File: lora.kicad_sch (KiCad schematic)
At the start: 2 parts

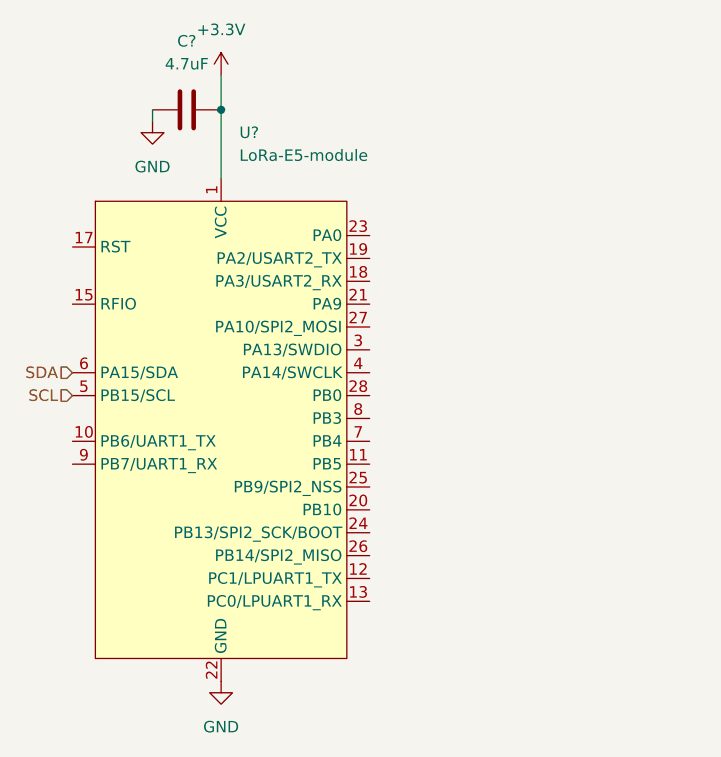
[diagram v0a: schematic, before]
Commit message: Added new lora, added rgb leds, updated TSP65988 schematic, added bat to 3v3, added battery balancer
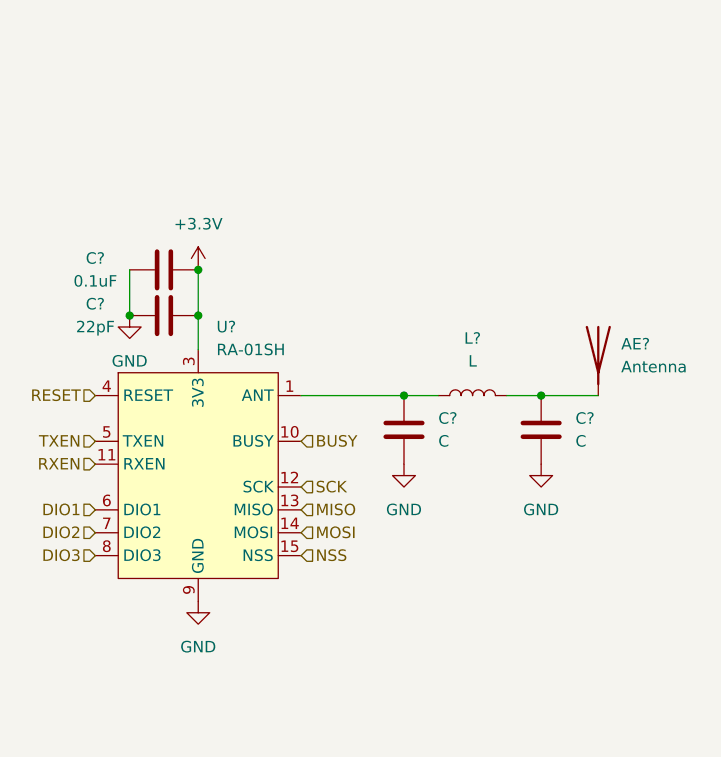
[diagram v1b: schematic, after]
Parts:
- removed C?: 4.7uF, symbol Device:C
- removed U?: LoRa-E5-module, airsoft_controller:LoRa-E5-module, symbol airsoft_controller:LoRa-E5-module
- added AE?: Antenna, symbol Device:Antenna
- added C?: 22pF, symbol Device:C
- added C? (x2): C, symbol Device:C
- added C?: 0.1uF, symbol Device:C
- added L?: L, symbol Device:L
- added U?: RA-01SH, symbol airsoft_controller:RA-01SH
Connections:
- net +3.3V: now also C?.2, C?.2, U?.3 (3V3)
- net GND: now also C?.1, C?.1, C?.2, C?.2, U?.16 (GND), U?.2 (GND), U?.9 (GND)
- new net: AE?.1 (A), C?.1, L?.2
- new net: C?.1, L?.1, U?.1 (ANT)
- new net BUSY: U?.10 (BUSY)
- new net DIO1: U?.6 (DIO1)
- new net DIO2: U?.7 (DIO2)
- new net DIO3: U?.8 (DIO3)
- new net MISO: U?.13 (MISO)
- new net MOSI: U?.14 (MOSI)
- new net NSS: U?.15 (NSS)
- new net RESET: U?.4 (RESET)
- new net RXEN: U?.11 (RXEN)
- new net SCK: U?.12 (SCK)
- new net TXEN: U?.5 (TXEN)

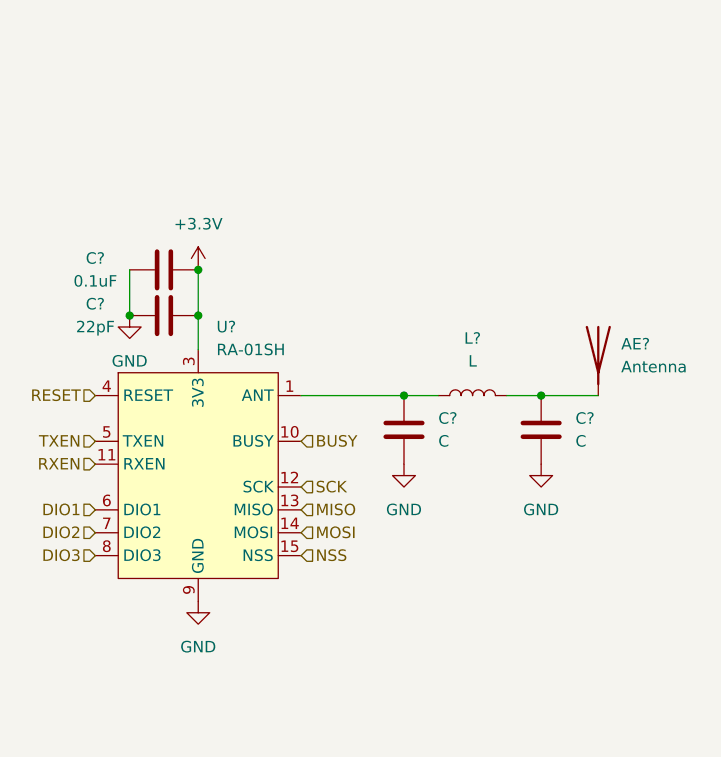
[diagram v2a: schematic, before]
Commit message: added audio ref schematic, added bat to 5V, added shift register, connected devices with other periferals
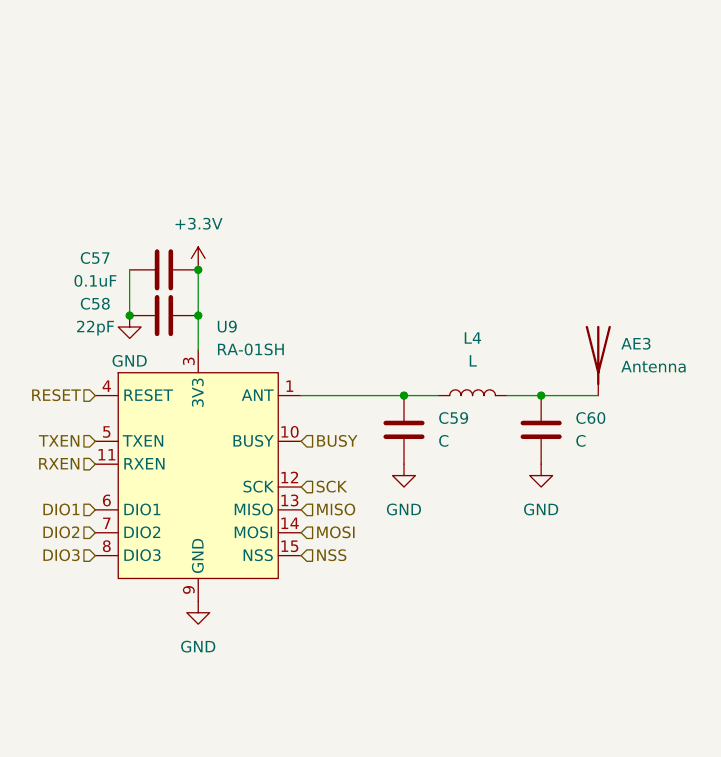
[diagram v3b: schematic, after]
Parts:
- gave numbers to parts that had none: 7
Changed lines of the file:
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@@
   (symbol (lib_id "Device:C") (at 143.51 83.82 90) (unit 1)
     (in_bom yes) (on_board yes)
-    (property "Reference" "C?" (id 0) (at 135.89 82.55 90))
+    (property "Reference" "C58" (id 0) (at 135.89 82.55 90))
     (property "Value" "22pF" (id 1) (at 135.89 85.09 90))
     (property "Footprint" "" (id 2) (at 147.32 82.8548 0)
@@
   (symbol (lib_id "Device:C") (at 185.42 96.52 0) (unit 1)
     (in_bom yes) (on_board yes) (fields_autoplaced)
-    (property "Reference" "C?" (id 0) (at 189.23 95.2499 0)
+    (property "Reference" "C60" (id 0) (at 189.23 95.2499 0)
       (effects (font (size 1.27 1.27)) (justify left))
     )
@@
   (symbol (lib_id "Device:Antenna") (at 191.77 87.63 0) (unit 1)
     (in_bom yes) (on_board yes) (fields_autoplaced)
-    (property "Reference" "AE?" (id 0) (at 194.31 86.9949 0)
+    (property "Reference" "AE3" (id 0) (at 194.31 86.9949 0)
       (effects (font (size 1.27 1.27)) (justify left))
     )
@@
   (symbol (lib_id "Device:C") (at 143.51 78.74 90) (unit 1)
     (in_bom yes) (on_board yes)
-    (property "Reference" "C?" (id 0) (at 135.89 77.47 90))
+    (property "Reference" "C57" (id 0) (at 135.89 77.47 90))
     (property "Value" "0.1uF" (id 1) (at 135.89 80.01 90))
     (property "Footprint" "" (id 2) (at 147.32 77.7748 0)
@@
   (symbol (lib_id "Device:C") (at 170.18 96.52 0) (unit 1)
     (in_bom yes) (on_board yes) (fields_autoplaced)
-    (property "Reference" "C?" (id 0) (at 173.99 95.2499 0)
+    (property "Reference" "C59" (id 0) (at 173.99 95.2499 0)
       (effects (font (size 1.27 1.27)) (justify left))
     )
@@
   (symbol (lib_id "Device:L") (at 177.8 92.71 90) (unit 1)
     (in_bom yes) (on_board yes) (fields_autoplaced)
-    (property "Reference" "L?" (id 0) (at 177.8 86.36 90))
+    (property "Reference" "L4" (id 0) (at 177.8 86.36 90))
     (property "Value" "L" (id 1) (at 177.8 88.9 90))
     (property "Footprint" "" (id 2) (at 177.8 92.71 0)
@@
   (symbol (lib_id "airsoft_controller:RA-01SH") (at 147.32 101.6 0) (unit 1)
     (in_bom yes) (on_board yes) (fields_autoplaced)
-    (property "Reference" "U?" (id 0) (at 149.3394 85.09 0)
+    (property "Reference" "U9" (id 0) (at 149.3394 85.09 0)
       (effects (font (size 1.27 1.27)) (justify left))
     )
@@
       (effects (font (size 1.27 1.27)) hide)
     )
-    (property "Datasheet" "" (id 3) (at 147.32 101.6 0)
+    (property "Datasheet" "https://docs.ai-thinker.com/_media/lora/docs/ra-01sh_specification.pdf" (id 3) (at 147.32 101.6 0)
       (effects (font (size 1.27 1.27)) hide)
     )

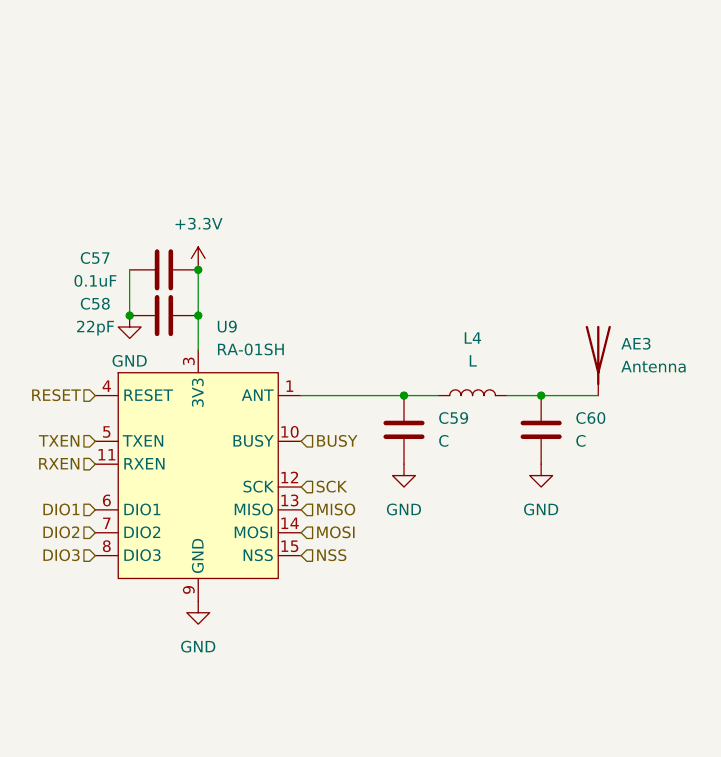
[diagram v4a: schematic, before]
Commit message: minor optimized pinassignement, added capacitors, added connectors
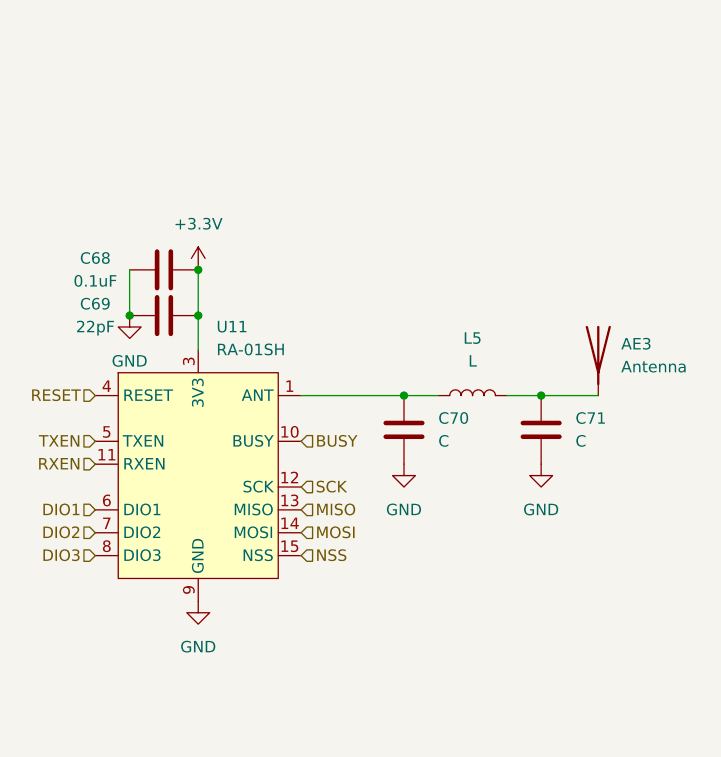
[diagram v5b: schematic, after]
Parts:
- renumbered C57 to C68, C58 to C69, C59 to C70, C60 to C71, L4 to L5, U9 to U11
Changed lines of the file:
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@@
   (symbol (lib_id "power:GND") (at 147.32 115.57 0) (unit 1)
     (in_bom yes) (on_board yes) (fields_autoplaced)
-    (property "Reference" "#PWR0172" (id 0) (at 147.32 121.92 0)
+    (property "Reference" "#PWR088" (id 0) (at 147.32 121.92 0)
       (effects (font (size 1.27 1.27)) hide)
     )
@@
   (symbol (lib_id "Device:C") (at 143.51 83.82 90) (unit 1)
     (in_bom yes) (on_board yes)
-    (property "Reference" "C58" (id 0) (at 135.89 82.55 90))
+    (property "Reference" "C69" (id 0) (at 135.89 82.55 90))
     (property "Value" "22pF" (id 1) (at 135.89 85.09 90))
     (property "Footprint" "" (id 2) (at 147.32 82.8548 0)
@@
   (symbol (lib_id "power:GND") (at 170.18 100.33 0) (unit 1)
     (in_bom yes) (on_board yes) (fields_autoplaced)
-    (property "Reference" "#PWR0169" (id 0) (at 170.18 106.68 0)
+    (property "Reference" "#PWR089" (id 0) (at 170.18 106.68 0)
       (effects (font (size 1.27 1.27)) hide)
     )
@@
   (symbol (lib_id "Device:C") (at 185.42 96.52 0) (unit 1)
     (in_bom yes) (on_board yes) (fields_autoplaced)
-    (property "Reference" "C60" (id 0) (at 189.23 95.2499 0)
+    (property "Reference" "C71" (id 0) (at 189.23 95.2499 0)
       (effects (font (size 1.27 1.27)) (justify left))
     )
@@
   (symbol (lib_id "power:GND") (at 185.42 100.33 0) (unit 1)
     (in_bom yes) (on_board yes) (fields_autoplaced)
-    (property "Reference" "#PWR0170" (id 0) (at 185.42 106.68 0)
+    (property "Reference" "#PWR090" (id 0) (at 185.42 106.68 0)
       (effects (font (size 1.27 1.27)) hide)
     )
@@
   (symbol (lib_id "power:GND") (at 139.7 83.82 0) (unit 1)
     (in_bom yes) (on_board yes) (fields_autoplaced)
-    (property "Reference" "#PWR0173" (id 0) (at 139.7 90.17 0)
+    (property "Reference" "#PWR086" (id 0) (at 139.7 90.17 0)
       (effects (font (size 1.27 1.27)) hide)
     )
@@
   (symbol (lib_id "Device:C") (at 143.51 78.74 90) (unit 1)
     (in_bom yes) (on_board yes)
-    (property "Reference" "C57" (id 0) (at 135.89 77.47 90))
+    (property "Reference" "C68" (id 0) (at 135.89 77.47 90))
     (property "Value" "0.1uF" (id 1) (at 135.89 80.01 90))
     (property "Footprint" "" (id 2) (at 147.32 77.7748 0)
@@
   (symbol (lib_id "Device:C") (at 170.18 96.52 0) (unit 1)
     (in_bom yes) (on_board yes) (fields_autoplaced)
-    (property "Reference" "C59" (id 0) (at 173.99 95.2499 0)
+    (property "Reference" "C70" (id 0) (at 173.99 95.2499 0)
       (effects (font (size 1.27 1.27)) (justify left))
     )
@@
   (symbol (lib_id "power:+3.3V") (at 147.32 78.74 0) (unit 1)
     (in_bom yes) (on_board yes) (fields_autoplaced)
-    (property "Reference" "#PWR0171" (id 0) (at 147.32 82.55 0)
+    (property "Reference" "#PWR087" (id 0) (at 147.32 82.55 0)
       (effects (font (size 1.27 1.27)) hide)
     )
@@
   (symbol (lib_id "Device:L") (at 177.8 92.71 90) (unit 1)
     (in_bom yes) (on_board yes) (fields_autoplaced)
-    (property "Reference" "L4" (id 0) (at 177.8 86.36 90))
+    (property "Reference" "L5" (id 0) (at 177.8 86.36 90))
     (property "Value" "L" (id 1) (at 177.8 88.9 90))
     (property "Footprint" "" (id 2) (at 177.8 92.71 0)
@@
   (symbol (lib_id "airsoft_controller:RA-01SH") (at 147.32 101.6 0) (unit 1)
     (in_bom yes) (on_board yes) (fields_autoplaced)
-    (property "Reference" "U9" (id 0) (at 149.3394 85.09 0)
+    (property "Reference" "U11" (id 0) (at 149.3394 85.09 0)
       (effects (font (size 1.27 1.27)) (justify left))
     )

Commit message: PI LC lowpass filter, added CP2012 reset, added connectors
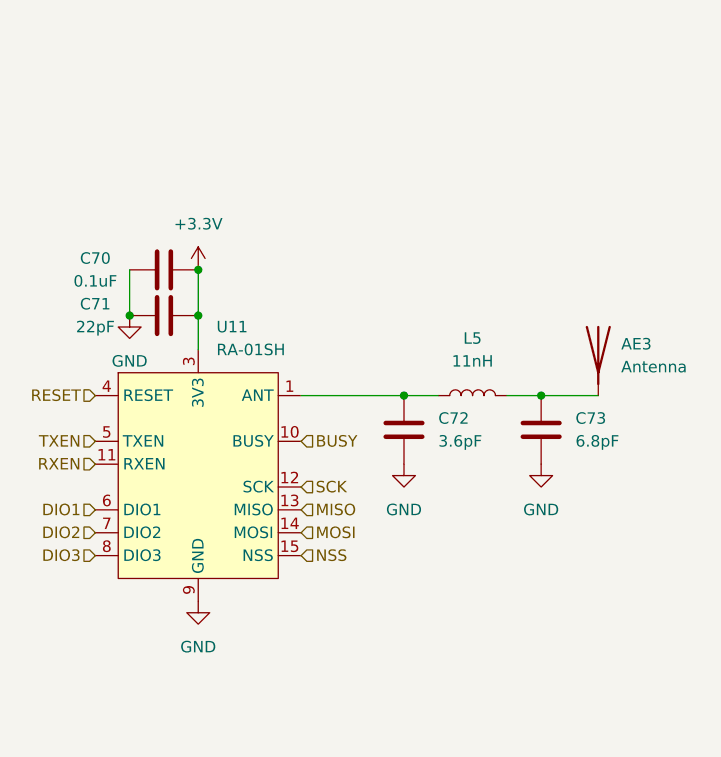
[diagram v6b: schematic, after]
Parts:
- C72: renamed from C70; value C -> 3.6pF
- C73: renamed from C71; value C -> 6.8pF
- L5: value L -> 11nH
- renumbered C68 to C70, C69 to C71
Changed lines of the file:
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@@
   (symbol (lib_id "power:GND") (at 147.32 115.57 0) (unit 1)
     (in_bom yes) (on_board yes) (fields_autoplaced)
-    (property "Reference" "#PWR088" (id 0) (at 147.32 121.92 0)
+    (property "Reference" "#PWR087" (id 0) (at 147.32 121.92 0)
       (effects (font (size 1.27 1.27)) hide)
     )
@@
   (symbol (lib_id "Device:C") (at 143.51 83.82 90) (unit 1)
     (in_bom yes) (on_board yes)
-    (property "Reference" "C69" (id 0) (at 135.89 82.55 90))
+    (property "Reference" "C71" (id 0) (at 135.89 82.55 90))
     (property "Value" "22pF" (id 1) (at 135.89 85.09 90))
     (property "Footprint" "" (id 2) (at 147.32 82.8548 0)
@@
   (symbol (lib_id "power:GND") (at 170.18 100.33 0) (unit 1)
     (in_bom yes) (on_board yes) (fields_autoplaced)
-    (property "Reference" "#PWR089" (id 0) (at 170.18 106.68 0)
+    (property "Reference" "#PWR088" (id 0) (at 170.18 106.68 0)
       (effects (font (size 1.27 1.27)) hide)
     )
@@
   (symbol (lib_id "Device:C") (at 185.42 96.52 0) (unit 1)
     (in_bom yes) (on_board yes) (fields_autoplaced)
-    (property "Reference" "C71" (id 0) (at 189.23 95.2499 0)
+    (property "Reference" "C73" (id 0) (at 189.23 95.2499 0)
       (effects (font (size 1.27 1.27)) (justify left))
     )
-    (property "Value" "C" (id 1) (at 189.23 97.7899 0)
+    (property "Value" "6.8pF" (id 1) (at 189.23 97.7899 0)
       (effects (font (size 1.27 1.27)) (justify left))
     )
@@
   (symbol (lib_id "power:GND") (at 185.42 100.33 0) (unit 1)
     (in_bom yes) (on_board yes) (fields_autoplaced)
-    (property "Reference" "#PWR090" (id 0) (at 185.42 106.68 0)
+    (property "Reference" "#PWR089" (id 0) (at 185.42 106.68 0)
       (effects (font (size 1.27 1.27)) hide)
     )
@@
   (symbol (lib_id "power:GND") (at 139.7 83.82 0) (unit 1)
     (in_bom yes) (on_board yes) (fields_autoplaced)
-    (property "Reference" "#PWR086" (id 0) (at 139.7 90.17 0)
+    (property "Reference" "#PWR085" (id 0) (at 139.7 90.17 0)
       (effects (font (size 1.27 1.27)) hide)
     )
@@
   (symbol (lib_id "Device:C") (at 143.51 78.74 90) (unit 1)
     (in_bom yes) (on_board yes)
-    (property "Reference" "C68" (id 0) (at 135.89 77.47 90))
+    (property "Reference" "C70" (id 0) (at 135.89 77.47 90))
     (property "Value" "0.1uF" (id 1) (at 135.89 80.01 90))
     (property "Footprint" "" (id 2) (at 147.32 77.7748 0)
@@
   (symbol (lib_id "Device:C") (at 170.18 96.52 0) (unit 1)
     (in_bom yes) (on_board yes) (fields_autoplaced)
-    (property "Reference" "C70" (id 0) (at 173.99 95.2499 0)
+    (property "Reference" "C72" (id 0) (at 173.99 95.2499 0)
       (effects (font (size 1.27 1.27)) (justify left))
     )
-    (property "Value" "C" (id 1) (at 173.99 97.7899 0)
+    (property "Value" "3.6pF" (id 1) (at 173.99 97.7899 0)
       (effects (font (size 1.27 1.27)) (justify left))
     )
@@
   (symbol (lib_id "power:+3.3V") (at 147.32 78.74 0) (unit 1)
     (in_bom yes) (on_board yes) (fields_autoplaced)
-    (property "Reference" "#PWR087" (id 0) (at 147.32 82.55 0)
+    (property "Reference" "#PWR086" (id 0) (at 147.32 82.55 0)
       (effects (font (size 1.27 1.27)) hide)
     )
@@
     (in_bom yes) (on_board yes) (fields_autoplaced)
     (property "Reference" "L5" (id 0) (at 177.8 86.36 90))
-    (property "Value" "L" (id 1) (at 177.8 88.9 90))
+    (property "Value" "11nH" (id 1) (at 177.8 88.9 90))
     (property "Footprint" "" (id 2) (at 177.8 92.71 0)
       (effects (font (size 1.27 1.27)) hide)
